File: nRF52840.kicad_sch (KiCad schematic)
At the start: 54 parts, among them J1 MM8130-2600RA2, J2 2X05, SW1 PTS840_GK_SMTR_LFS, U4 NRF52840, U8 BME280, Y2 ABM11W-101-32.0000MHZ-T3, Y3 ABS06-32.768KHZ-9-1-T

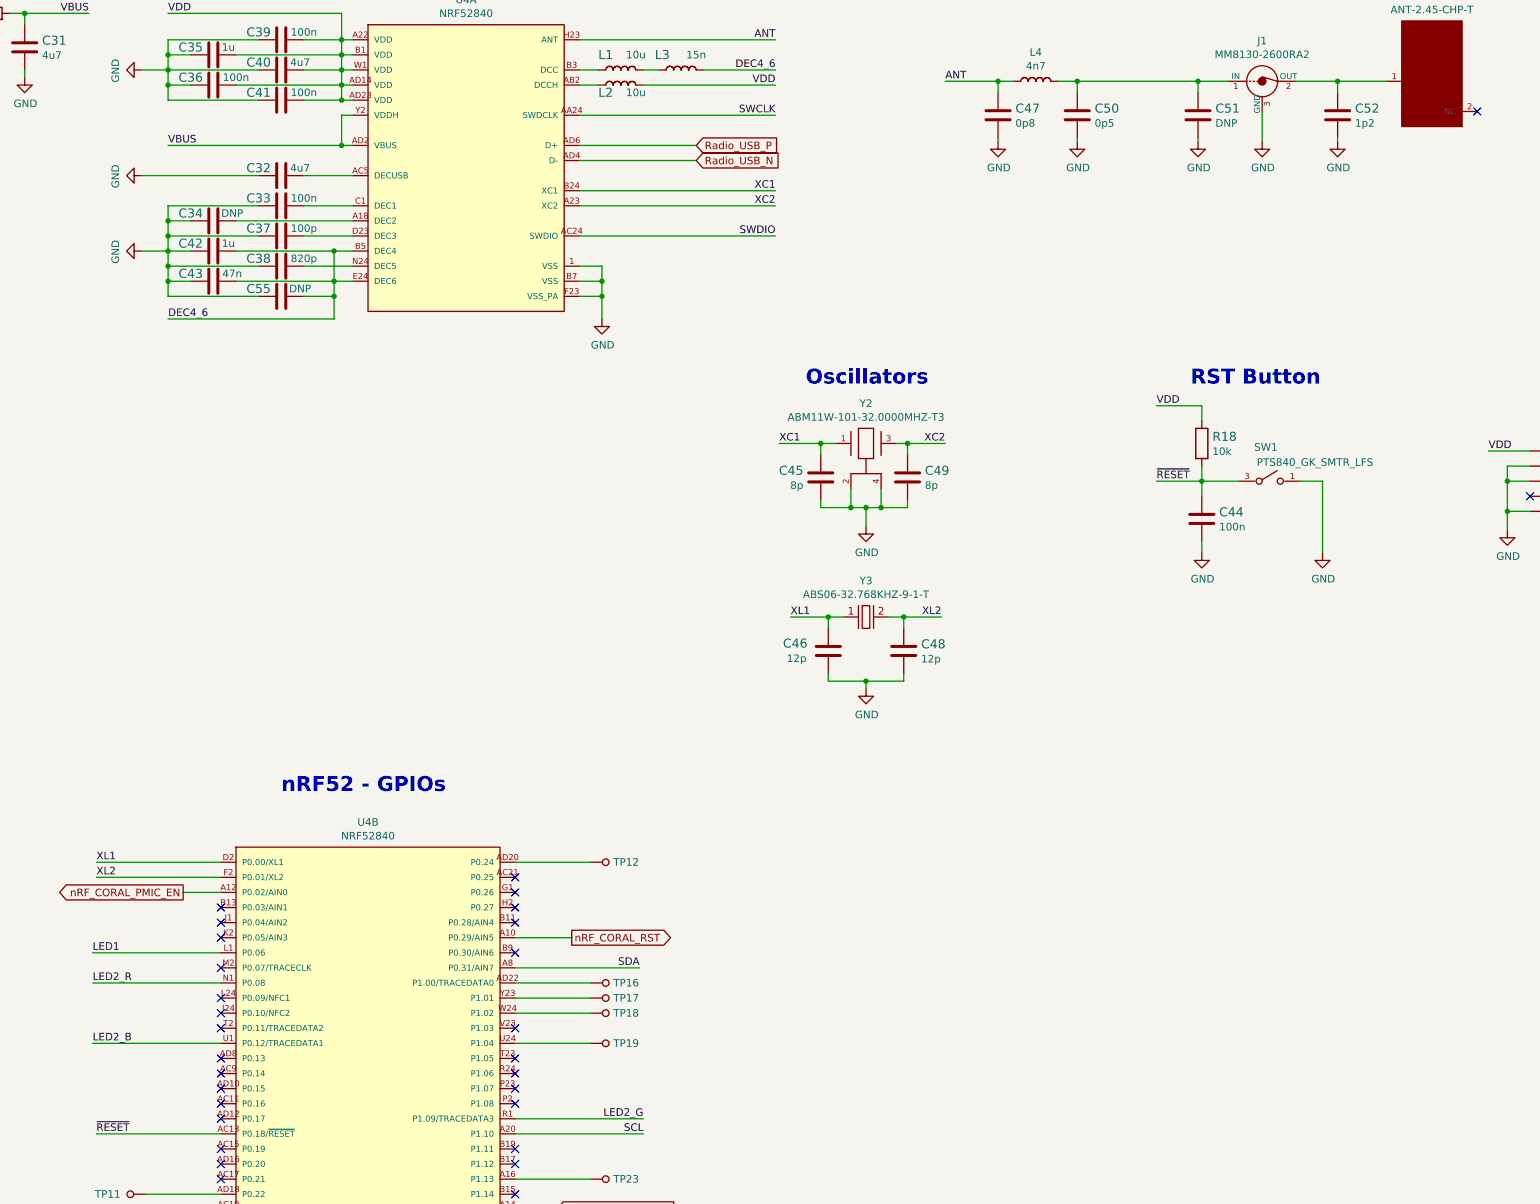
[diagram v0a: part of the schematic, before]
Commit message: Added FTDI schematic
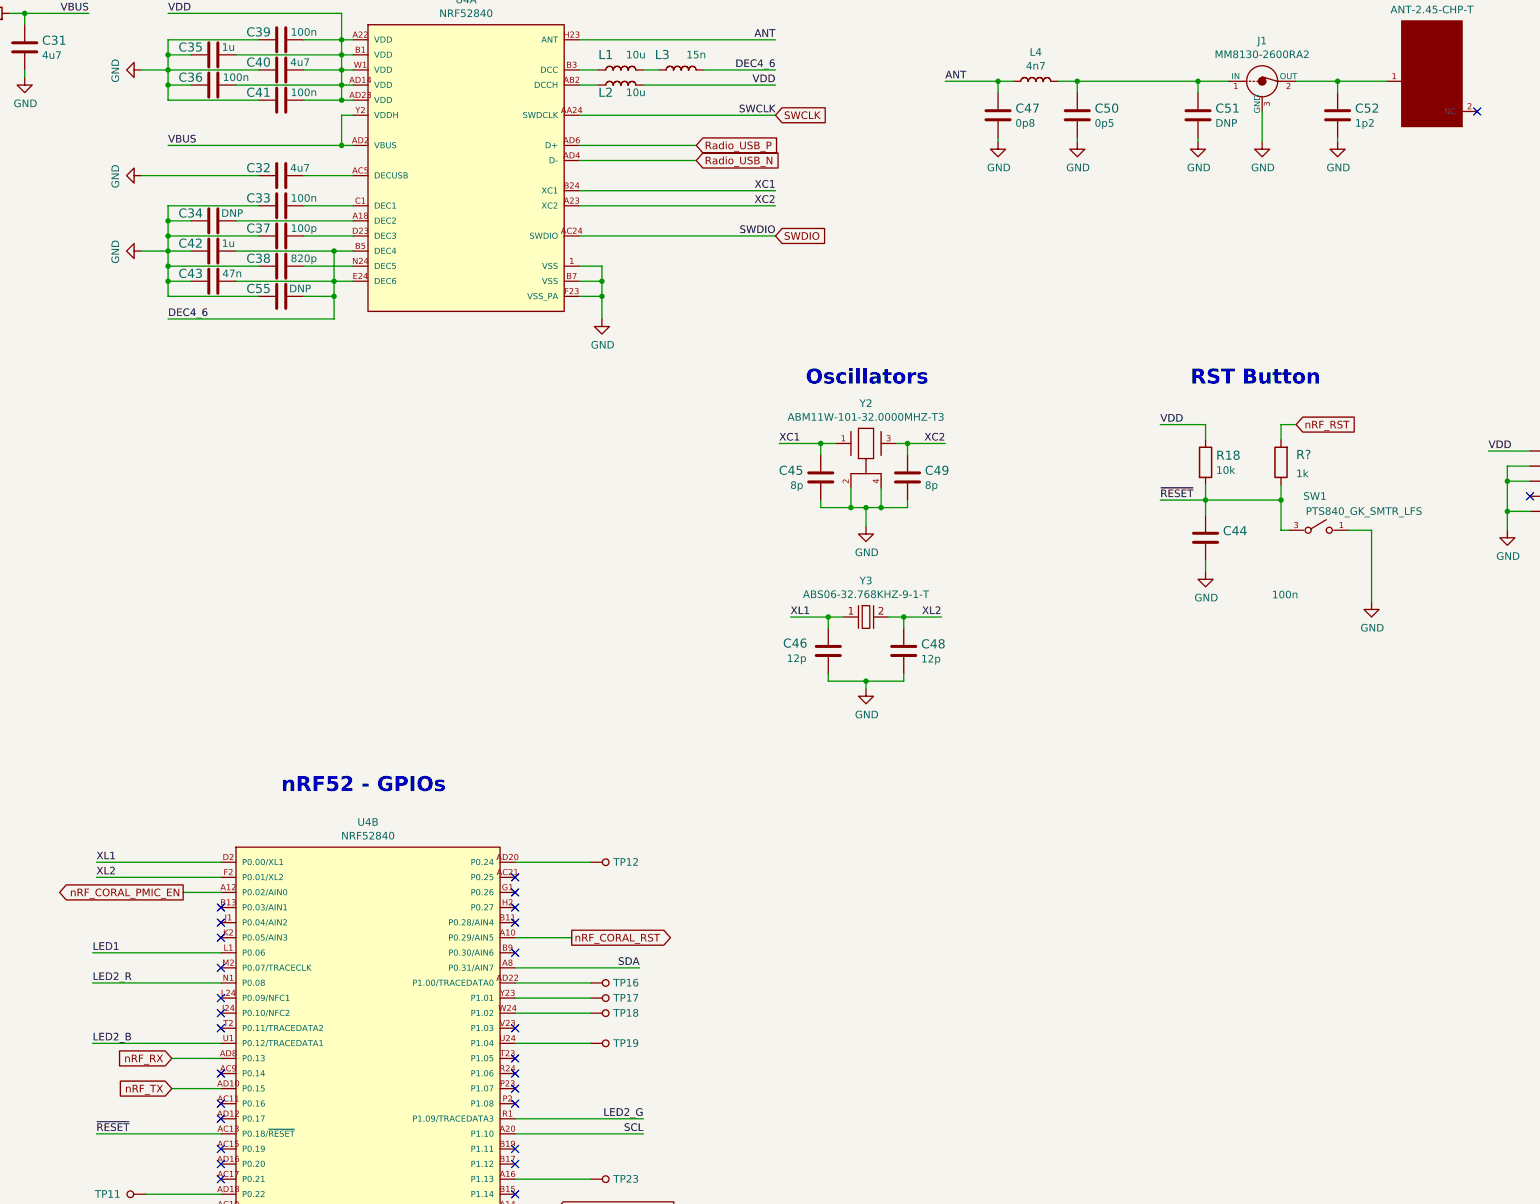
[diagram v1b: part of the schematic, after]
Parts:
- added R?: R_1k_0402, antmicro-footprints:0402-res, symbol antmicroResistors0402:R_1k_0402
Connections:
- net ~{RESET}: now also R?.1
- net nRF_TX: now reaches U4.AD10 (P0.15)
- net nRF_RX: now reaches U4.AD8 (P0.13)
- new net nRF_RST: R?.2
- no-connect marks 33 -> 31
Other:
- moved on the sheet: C44, R18, SW1

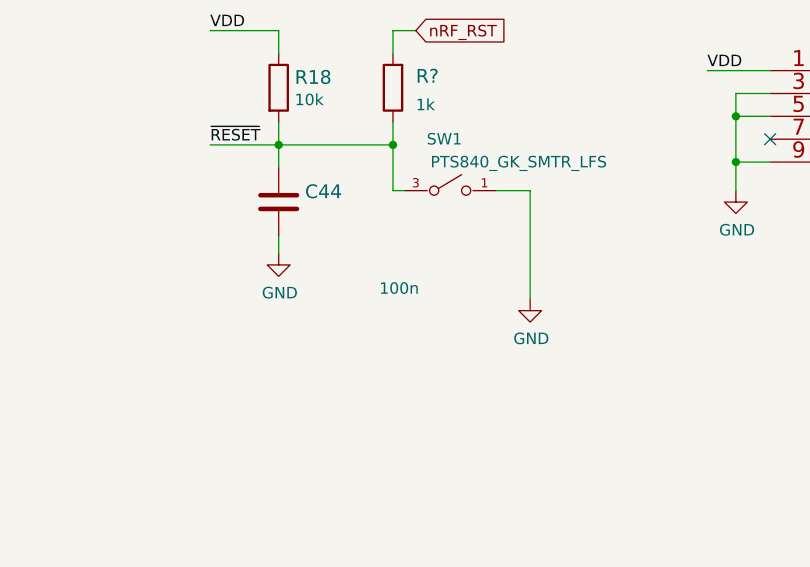
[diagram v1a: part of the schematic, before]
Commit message: Added comments to schematic
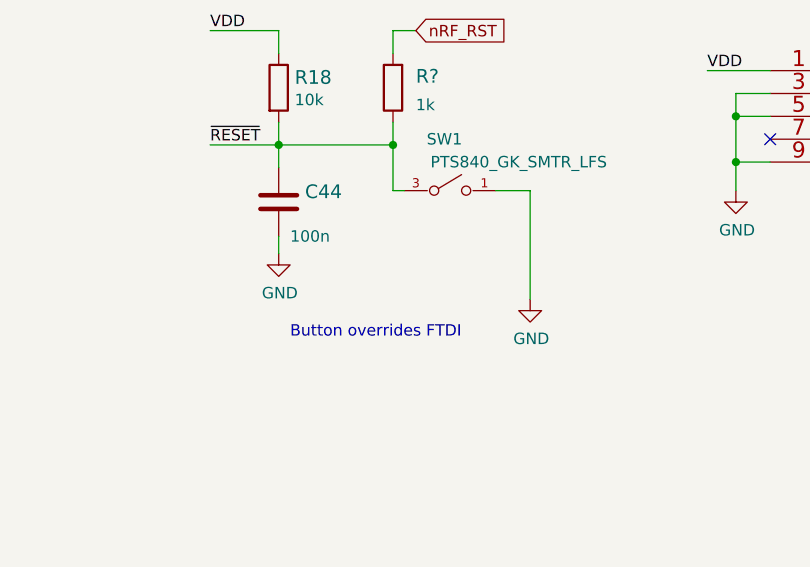
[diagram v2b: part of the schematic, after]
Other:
- note added: "Button overrides FTDI"
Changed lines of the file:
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@@
     (stroke (width 0) (type default) (color 0 0 0 0))
+  )
+  (text "Button overrides FTDI" (at 234.95 152.4 0)
+    (effects (font (size 1.27 1.27)) (justify left bottom))
   )
   (text "CSB pulled up -> I2C communication (current option)\nCSB pulled down -> SPI communication\n\nSDO pulled down -> I2C addr: 0x76\nSDO pulled up -> I2C addr: 0x77 (current option)"
@@
       (effects (font (size 1.524 1.524)) (justify left) hide)
     )
-    (property "Val" "100n" (id 6) (at 244.856 146.7612 0)
+    (property "Val" "100n" (id 6) (at 234.95 140.97 0)
       (effects (font (size 1.27 1.27)) (justify left))
     )

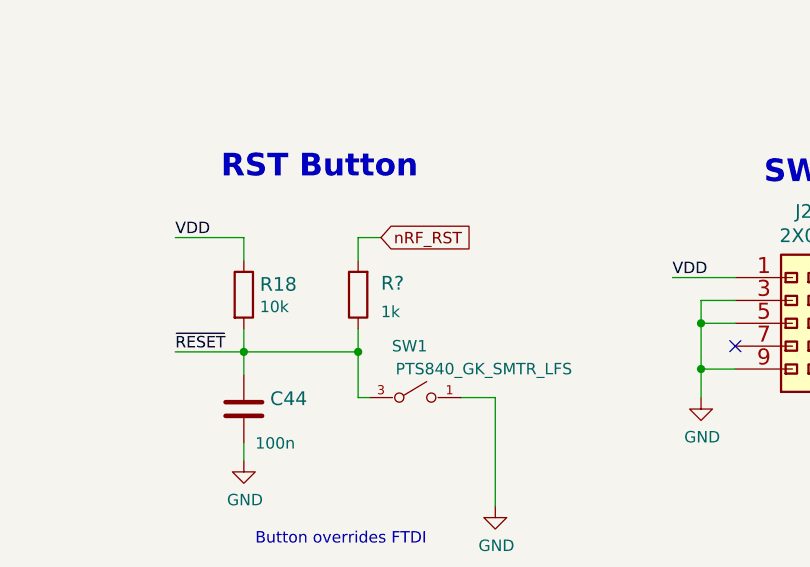
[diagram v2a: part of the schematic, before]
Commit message: Created FT2232 layout
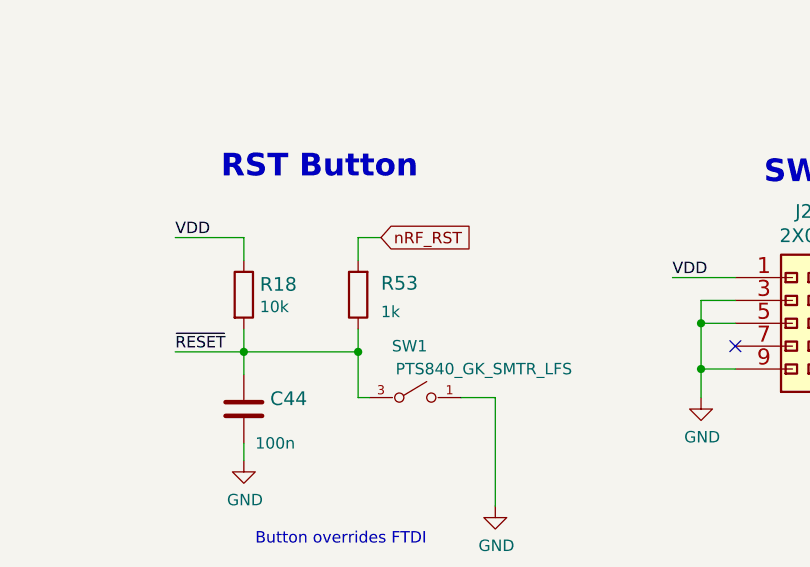
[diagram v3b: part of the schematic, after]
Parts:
- J2, SW1: DNP (none) -> DNP
- gave numbers to parts that had none: 1
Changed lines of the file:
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@@
   (title_block
     (title "M.2 Smart IoT Module")
-    (date "2021-08-11")
-    (rev "1.1.0")
+    (date "2022-07-11")
+    (rev "1.2.0")
     (comment 1 "www.antmicro.com")
     (comment 2 "Antmicro Ltd.")
@@
       (effects (font (size 1.27 1.27)) hide)
     )
+    (property "DNP" "DNP" (id 6) (at 247.65 130.81 0)
+      (effects (font (size 1.27 1.27)) hide)
+    )
     (pin "1")
     (pin "2")
@@
     )
     (property "Manufacturer" "Samtec" (id 5) (at 290.83 144.145 0)
+      (effects (font (size 1.27 1.27)) hide)
+    )
+    (property "DNP" "DNP" (id 6) (at 295.91 122.555 0)
       (effects (font (size 1.27 1.27)) hide)
     )
@@
   (symbol (lib_id "antmicroResistors0402:R_1k_0402") (at 246.38 124.46 90) (unit 1)
     (in_bom yes) (on_board yes) (fields_autoplaced)
-    (property "Reference" "R?" (id 0) (at 248.92 123.19 90)
+    (property "Reference" "R53" (id 0) (at 248.92 123.19 90)
       (effects (font (size 1.524 1.524)) (justify right))
     )
